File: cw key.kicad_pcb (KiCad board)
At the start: 2 copper layers, 39 x 31.5 mm, 40 parts, among them J1 AudioPlug3, J2 Conn_01x01_Pin, J3 Conn_01x01_Pin, J4 Conn_ARM_SWD_TagConnect_TC203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, J5 AudioPlug3, J6 Conn_01x01_Pin, J7 Conn_01x01_Pin, SW3 SW_SPST, U1 MSPM0C1103SDSGR, U2 MTCH1030

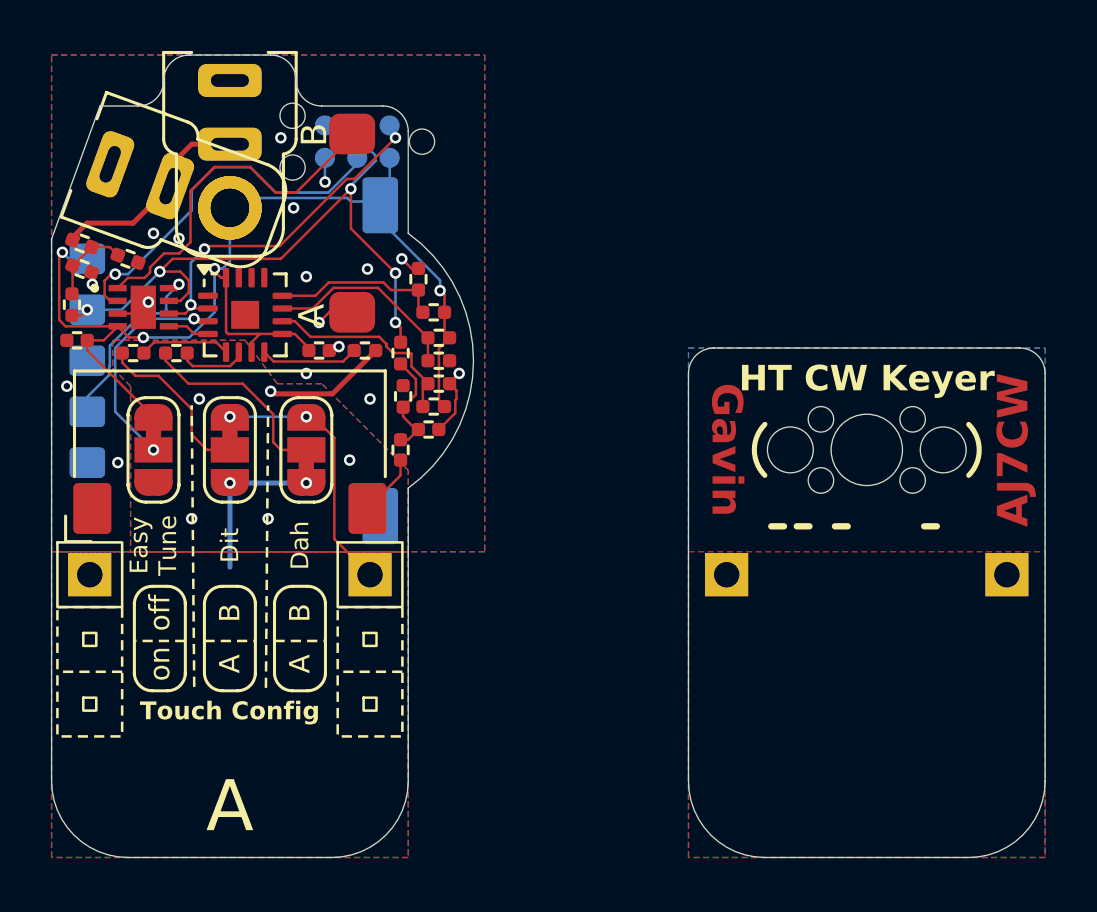
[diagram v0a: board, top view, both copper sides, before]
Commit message: updated to use 4 pin 3.5mm jack
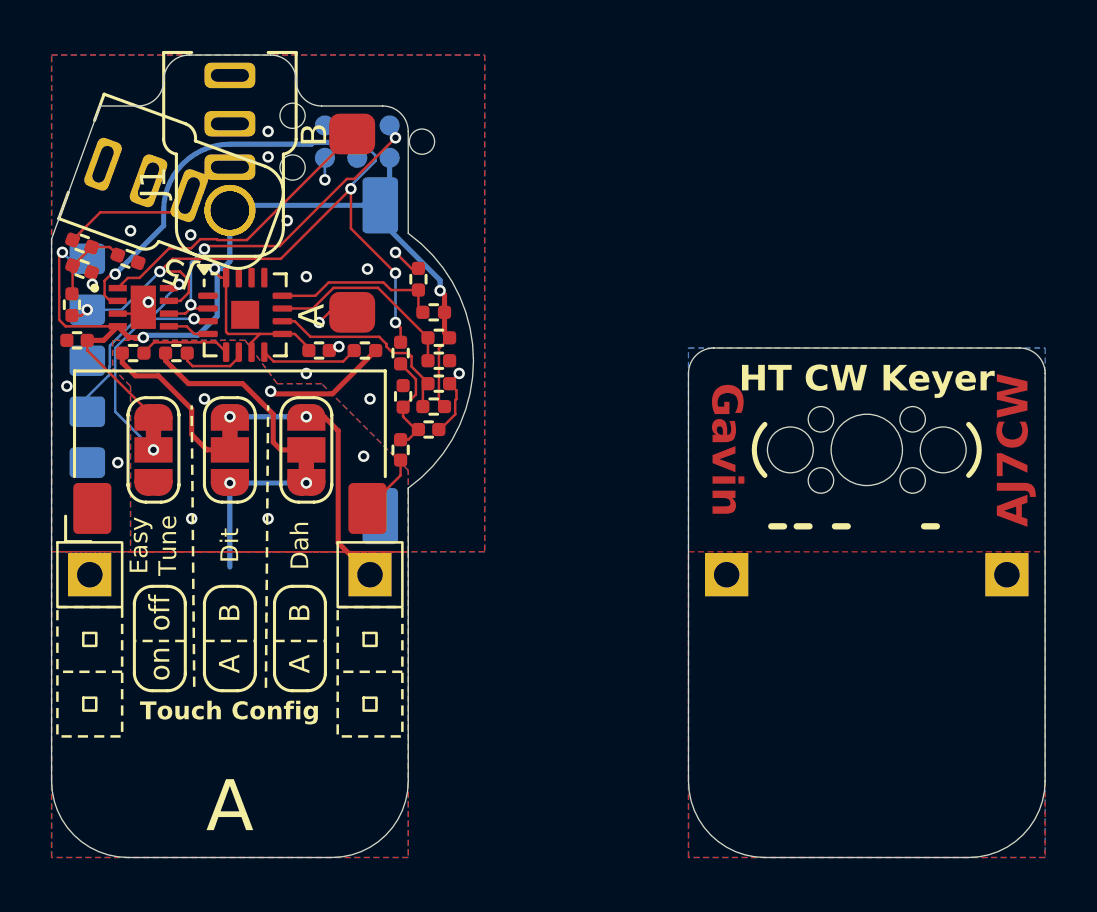
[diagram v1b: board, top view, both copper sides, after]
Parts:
- J1, J5: footprint footprints:3.5 mm plug -> footprints:3.5 mm plug 4 pin
- moved J5 0.11 mm to (144.3, 71.0)
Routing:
- net RST: track 14.5 -> 10.3 mm
- net Net-(C1-Pad1): track 8.26 -> 5.42 mm
- net A_B_Switch: track 13.9 -> 11.8 mm
- net GND: track 8.00 -> 8.32 mm, vias 17 -> 18

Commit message: melted
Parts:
- moved J6 11.0 mm to (180.5, 87.4)
- moved J7 11.0 mm to (169.5, 87.4)
- moved C2 0.54 mm to (144.2, 78.7)
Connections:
- J6 pad 1: /GND_shield -> /pad_0
- J7 pad 1: /pad_0 -> /GND_shield
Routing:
- net /GND_shield: track 4.87 -> 2.70 mm
- net CLK: track 25.7 -> 24.2 mm
- net GND: track 8.32 -> 7.50 mm
- net Net-(JP3-C): track 8.77 -> 8.09 mm
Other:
- board text added: "QRM Generator"
- board text removed: "QRM generator"
